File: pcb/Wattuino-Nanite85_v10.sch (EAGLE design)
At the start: 18 parts, among them IC2 ATTINY85-MU, J1 USB-MICRO, J2 MA04-1, J3 MA04-1, SW1 SW-TACTILE-PTS840P, X1 PASSER-07, X2 PASSER-07, X3 PASSER-07

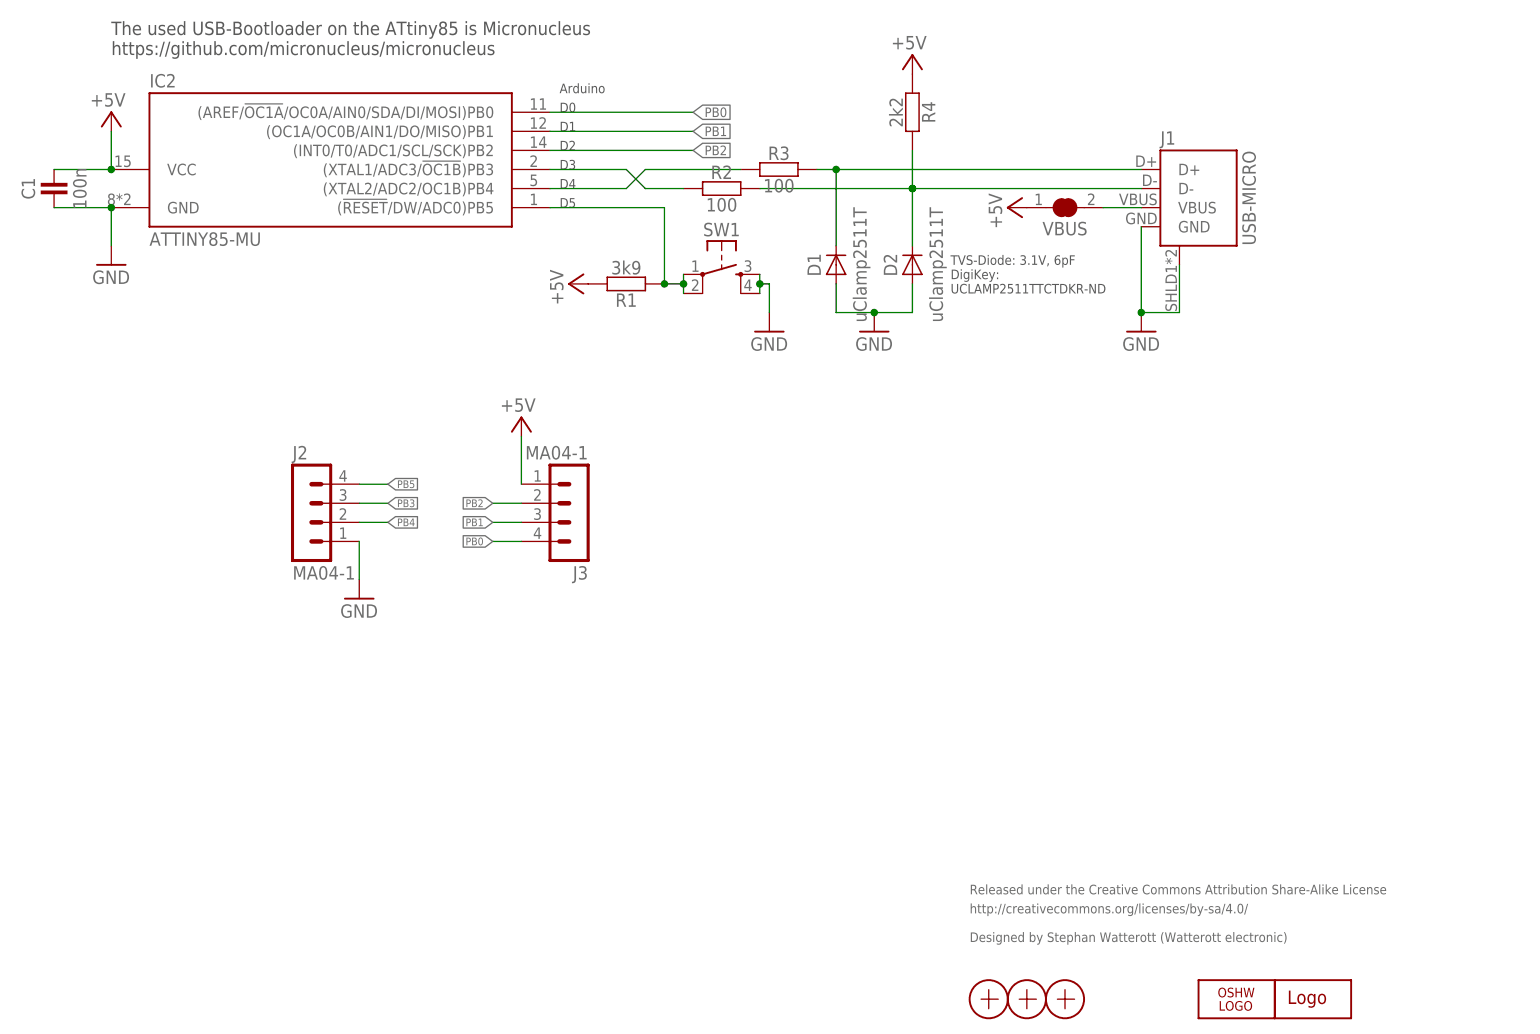
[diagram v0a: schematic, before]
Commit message: updated Tiny85/Nanite85
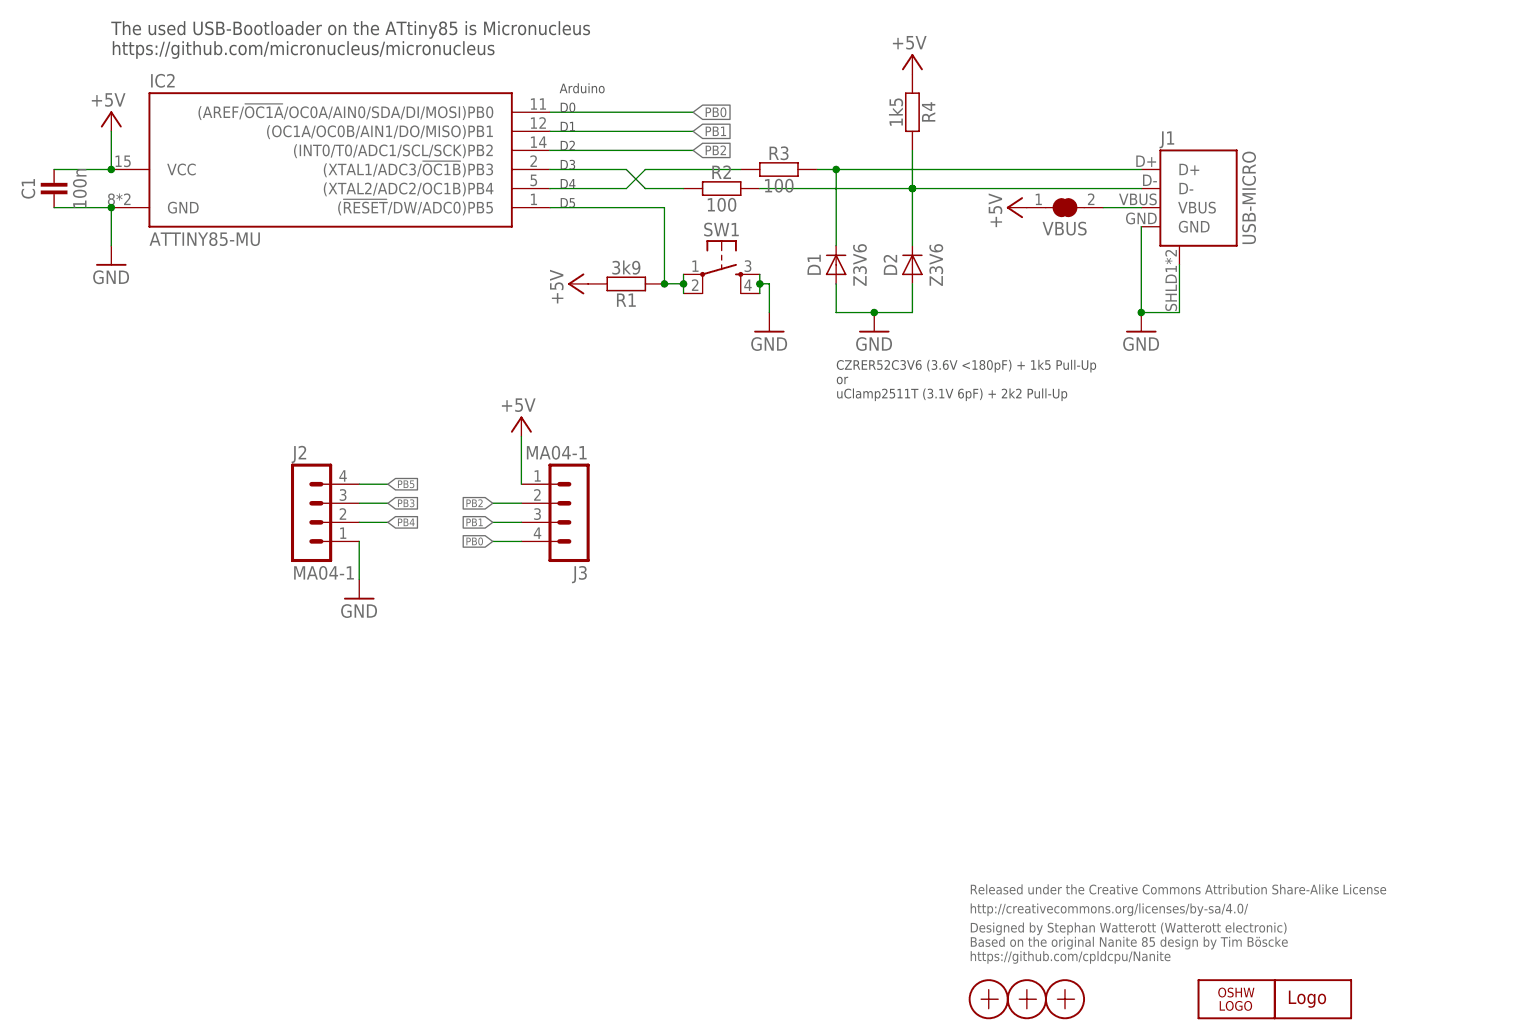
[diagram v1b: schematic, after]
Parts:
- D1, D2: value uClamp2511T -> Z3V6
- R4: value 2k2 -> 1k5
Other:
- note added: "CZRER52C3V6 (3.6V <180pF) + 1k5 Pull-Up or uClamp2511T (3.1V 6pF) + 2k2 Pull-Up"
- note added: "Designed by Stephan Watterott (Watterott electronic) Based on the original Nanite 85 design by Tim Böscke https://github.com/cpldcpu/Nanite"
- note removed: "Designed by Stephan Watterott (Watterott electronic)"
- note removed: "TVS-Diode: 3.1V, 6pF DigiKey: UCLAMP2511TTCTDKR-ND"
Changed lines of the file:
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@@
 <part name="GND17" library="supply1" deviceset="GND" device=""/>
 <part name="GND19" library="supply1" deviceset="GND" device=""/>
-<part name="R4" library="we-rcl" deviceset="RESISTOR" device="-R0402" value="2k2"/>
+<part name="R4" library="we-rcl" deviceset="RESISTOR" device="-R0402" value="1k5"/>
 <part name="GND20" library="supply1" deviceset="GND" device=""/>
 <part name="P+15" library="supply1" deviceset="+5V" device=""/>
@@
 <part name="R1" library="we-rcl" deviceset="RESISTOR" device="-R0402" value="3k9"/>
 <part name="P+16" library="supply1" deviceset="+5V" device=""/>
-<part name="D2" library="we-rcl" deviceset="DIODE" device="-SOD882" value="uClamp2511T"/>
-<part name="D1" library="we-rcl" deviceset="DIODE" device="-SOD882" value="uClamp2511T"/>
+<part name="D2" library="we-rcl" deviceset="DIODE" device="-SOD882" value="Z3V6"/>
+<part name="D1" library="we-rcl" deviceset="DIODE" device="-SOD882" value="Z3V6"/>
 <part name="GND15" library="supply1" deviceset="GND" device=""/>
 <part name="P+10" library="supply1" deviceset="+5V" device=""/>
@@
 <text x="162.56" y="21.59" size="1.27" layer="95">Released under the Creative Commons Attribution Share-Alike License</text>
 <text x="162.56" y="19.05" size="1.27" layer="95">http://creativecommons.org/licenses/by-sa/4.0/</text>
-<text x="162.56" y="15.24" size="1.27" layer="95">Designed by Stephan Watterott (Watterott electronic)</text>
+<text x="162.56" y="12.7" size="1.27" layer="95">Designed by Stephan Watterott (Watterott electronic)
+Based on the original Nanite 85 design by Tim Böscke
+https://github.com/cpldcpu/Nanite</text>
 <wire x1="174.625" y1="113.03" x2="175.895" y2="113.03" width="0.4064" layer="94"/>
 <text x="48.26" y="133.35" size="1.778" layer="97">The used USB-Bootloader on the ATtiny85 is Micronucleus
 https://github.com/micronucleus/micronucleus</text>
-<text x="160.02" y="101.6" size="1.27" layer="97">TVS-Diode: 3.1V, 6pF
-DigiKey:
-UCLAMP2511TTCTDKR-ND</text>
+<text x="144.78" y="87.63" size="1.27" layer="97">CZRER52C3V6 (3.6V &lt;180pF) + 1k5 Pull-Up
+or
+uClamp2511T (3.1V 6pF) + 2k2 Pull-Up</text>
 <text x="107.95" y="128.27" size="1.27" layer="97">Arduino</text>
 <text x="107.95" y="125.73" size="1.27" layer="97">D0</text>

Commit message: updated layout and schematics
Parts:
- C1: device we-rcl:CAPACITOR-C0402 -> we-rcl:CAPACITOR-0402
- R1, R2, R3, R4: device we-rcl:RESISTOR-R0402 -> we-rcl:RESISTOR-0402
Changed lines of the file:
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@@
 <?xml version="1.0" encoding="utf-8"?>
 <!DOCTYPE eagle SYSTEM "eagle.dtd">
-<eagle version="6.6.0">
+<eagle version="7.2.0">
 <drawing>
 <settings>
@@
 <layer number="48" name="Document" color="7" fill="1" visible="no" active="no"/>
 <layer number="49" name="Reference" color="7" fill="1" visible="no" active="no"/>
-<layer number="50" name="dxf" color="7" fill="1" visible="no" active="no"/>
 <layer number="51" name="tDocu" color="7" fill="1" visible="no" active="no"/>
 <layer number="52" name="bDocu" color="7" fill="1" visible="no" active="no"/>
-<layer number="53" name="tCopper" color="7" fill="11" visible="no" active="no"/>
-<layer number="54" name="bCopper" color="7" fill="1" visible="no" active="no"/>
-<layer number="56" name="wert" color="7" fill="1" visible="no" active="no"/>
-<layer number="57" name="tCAD" color="7" fill="1" visible="no" active="no"/>
+<layer number="90" name="Modules" color="5" fill="1" visible="yes" active="yes"/>
 <layer number="91" name="Nets" color="2" fill="1" visible="yes" active="yes"/>
 <layer number="92" name="Busses" color="1" fill="1" visible="yes" active="yes"/>
@@
 <layer number="98" name="Guide" color="6" fill="1" visible="yes" active="yes"/>
 <layer number="99" name="SpiceOrder" color="5" fill="1" visible="yes" active="yes"/>
-<layer number="100" name="Muster" color="7" fill="1" visible="no" active="no"/>
-<layer number="153" name="FabDoc1" color="6" fill="1" visible="no" active="no"/>
-<layer number="154" name="FabDoc2" color="2" fill="1" visible="no" active="no"/>
-<layer number="155" name="FabDoc3" color="7" fill="15" visible="no" active="no"/>
-<layer number="200" name="200bmp" color="1" fill="10" visible="no" active="no"/>
-<layer number="217" name="217bmp" color="18" fill="1" visible="no" active="no"/>
-<layer number="218" name="218bmp" color="19" fill="1" visible="no" active="no"/>
-<layer number="219" name="219bmp" color="20" fill="1" visible="no" active="no"/>
-<layer number="220" name="220bmp" color="21" fill="1" visible="no" active="no"/>
-<layer number="221" name="221bmp" color="22" fill="1" visible="no" active="no"/>
-<layer number="222" name="222bmp" color="23" fill="1" visible="no" active="no"/>
-<layer number="223" name="223bmp" color="24" fill="1" visible="no" active="no"/>
-<layer number="224" name="224bmp" color="25" fill="1" visible="no" active="no"/>
-<layer number="250" name="Descript" color="3" fill="1" visible="yes" active="yes"/>
-<layer number="251" name="SMDround" color="12" fill="11" visible="no" active="no"/>
 </layers>
 <schematic xreflabel="%F%N/%S.%C%R" xrefpart="/%S.%C%R">
@@
 <part name="LOGO2" library="we-symbol" deviceset="OSHW_LOGO" device="X0070" value="OSHW_LOGOX0070"/>
 <part name="X3" library="we-symbol" deviceset="PASSER" device="-07"/>
-<part name="C1" library="we-rcl" deviceset="CAPACITOR" device="-C0402" value="100n"/>
+<part name="C1" library="we-rcl" deviceset="CAPACITOR" device="-0402" value="100n"/>
 <part name="LOGO1" library="we-symbol" deviceset="LOGO" device="-S_PLACE_S" value="LOGO-S_PLACE_S"/>
 <part name="FRAME1" library="we-symbol" deviceset="FRAME-A4L" device=""/>
 <part name="IC2" library="we-chip" deviceset="ATTINY85" device="-MU"/>
 <part name="J1" library="we-con" deviceset="USB" device="-MICRO"/>
-<part name="R3" library="we-rcl" deviceset="RESISTOR" device="-R0402" value="100"/>
-<part name="R2" library="we-rcl" deviceset="RESISTOR" device="-R0402" value="100"/>
+<part name="R3" library="we-rcl" deviceset="RESISTOR" device="-0402" value="100"/>
+<part name="R2" library="we-rcl" deviceset="RESISTOR" device="-0402" value="100"/>
 <part name="GND17" library="supply1" deviceset="GND" device=""/>
 <part name="GND19" library="supply1" deviceset="GND" device=""/>
-<part name="R4" library="we-rcl" deviceset="RESISTOR" device="-R0402" value="1k5"/>
+<part name="R4" library="we-rcl" deviceset="RESISTOR" device="-0402" value="1k5"/>
 <part name="GND20" library="supply1" deviceset="GND" device=""/>
 <part name="P+15" library="supply1" deviceset="+5V" device=""/>
 <part name="VBUS" library="we-rcl" deviceset="JUMPER2" device="-0603-NC" value="JUMPER2-0603-NC"/>
 <part name="P+11" library="supply1" deviceset="+5V" device=""/>
-<part name="R1" library="we-rcl" deviceset="RESISTOR" device="-R0402" value="3k9"/>
+<part name="R1" library="we-rcl" deviceset="RESISTOR" device="-0402" value="3k9"/>
 <part name="P+16" library="supply1" deviceset="+5V" device=""/>
 <part name="D2" library="we-rcl" deviceset="DIODE" device="-SOD882" value="Z3V6"/>

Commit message: updated schematics
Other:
- note added: "GND"
- note added: "VCC"
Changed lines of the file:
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@@
 <?xml version="1.0" encoding="utf-8"?>
 <!DOCTYPE eagle SYSTEM "eagle.dtd">
-<eagle version="7.2.0">
+<eagle version="7.3.0">
 <drawing>
 <settings>
@@
 <setting verticaltext="up"/>
 </settings>
-<grid distance="0.1" unitdist="inch" unit="inch" style="lines" multiple="1" display="no" altdistance="0.01" altunitdist="inch" altunit="inch"/>
+<grid distance="0.05" unitdist="inch" unit="inch" style="lines" multiple="1" display="yes" altdistance="0.025" altunitdist="inch" altunit="inch"/>
 <layers>
 <layer number="1" name="Top" color="4" fill="1" visible="no" active="no"/>
@@
 <text x="107.95" y="113.03" size="1.27" layer="97">D5</text>
 <text x="72.39" y="142.24" size="3.81" layer="250">ATtiny85 AVR</text>
+<text x="113.03" y="68.58" size="1.778" layer="97" align="center-left">D0</text>
+<text x="113.03" y="71.12" size="1.778" layer="97" align="center-left">D1</text>
+<text x="113.03" y="73.66" size="1.778" layer="97" align="center-left">D2</text>
+<text x="69.85" y="76.2" size="1.778" layer="97" rot="R180" align="center-left">D5</text>
+<text x="69.85" y="73.66" size="1.778" layer="97" rot="R180" align="center-left">D3</text>
+<text x="69.85" y="71.12" size="1.778" layer="97" rot="R180" align="center-left">D4</text>
+<text x="69.85" y="68.58" size="1.778" layer="97" rot="R180" align="center-left">GND</text>
+<text x="113.03" y="76.2" size="1.778" layer="97" align="center-left">VCC</text>
 </plain>
 <instances>
@@
 </segment>
 <segment>
-<label x="85.09" y="73.66" size="1.016" layer="95" xref="yes"/>
+<label x="85.09" y="73.66" size="1.27" layer="95" xref="yes"/>
 <pinref part="J2" gate="J" pin="3"/>
 <wire x1="85.09" y1="73.66" x2="81.28" y2="73.66" width="0.1524" layer="91"/>
@@
 </segment>
 <segment>
-<label x="85.09" y="71.12" size="1.016" layer="95" xref="yes"/>
+<label x="85.09" y="71.12" size="1.27" layer="95" xref="yes"/>
 <pinref part="J2" gate="J" pin="2"/>
 <wire x1="85.09" y1="71.12" x2="81.28" y2="71.12" width="0.1524" layer="91"/>
@@
 <pinref part="J3" gate="J" pin="4"/>
 <wire x1="102.87" y1="68.58" x2="99.06" y2="68.58" width="0.1524" layer="91"/>
-<label x="99.06" y="68.58" size="1.016" layer="95" rot="R180" xref="yes"/>
+<label x="99.06" y="68.58" size="1.27" layer="95" rot="R180" xref="yes"/>
 </segment>
 </net>
@@
 <pinref part="J3" gate="J" pin="2"/>
 <wire x1="102.87" y1="73.66" x2="99.06" y2="73.66" width="0.1524" layer="91"/>
-<label x="99.06" y="73.66" size="1.016" layer="95" rot="R180" xref="yes"/>
+<label x="99.06" y="73.66" size="1.27" layer="95" rot="R180" xref="yes"/>
 </segment>
 </net>
@@
 <pinref part="J3" gate="J" pin="3"/>
 <wire x1="102.87" y1="71.12" x2="99.06" y2="71.12" width="0.1524" layer="91"/>
-<label x="99.06" y="71.12" size="1.016" layer="95" rot="R180" xref="yes"/>
+<label x="99.06" y="71.12" size="1.27" layer="95" rot="R180" xref="yes"/>
 </segment>
 </net>
@@
 <pinref part="J2" gate="J" pin="4"/>
 <wire x1="81.28" y1="76.2" x2="85.09" y2="76.2" width="0.1524" layer="91"/>
-<label x="85.09" y="76.2" size="1.016" layer="95" xref="yes"/>
-</segment>
-</net>
+<label x="85.09" y="76.2" size="1.27" layer="95" xref="yes"/>
+</segment>
+</net>
